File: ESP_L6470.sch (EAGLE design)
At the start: 39 parts, among them IC2 CP2104, J1 MICRO-USB, J2 POWER_JACKPTH_LOCK, Q1 600mA/40V, Q2 600mA/40V, U1 L6470, U2 ESP-WROOM-03, U3 RGB-LED

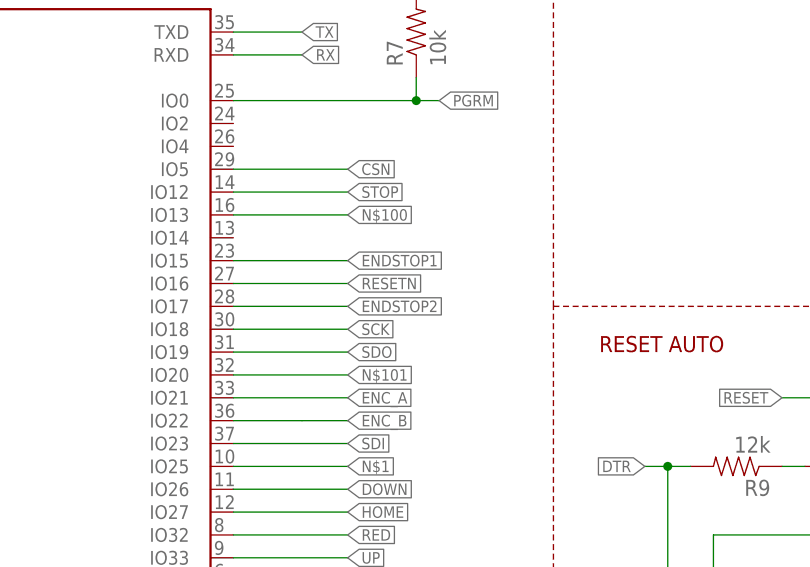
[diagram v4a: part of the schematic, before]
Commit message: Updated with silkscreen
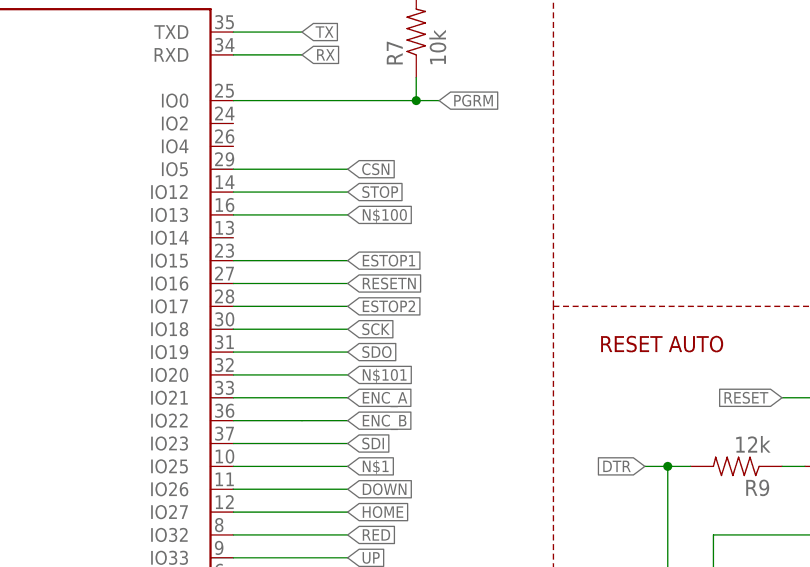
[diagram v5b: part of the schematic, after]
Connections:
- new net ESTOP1: U2.IO15
- new net ESTOP2: U2.IO17
- net ENDSTOP1: no longer U2.IO15
- net ENDSTOP2: no longer U2.IO17
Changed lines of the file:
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@@
 <label x="320.04" y="66.04" size="1.27" layer="95" rot="R180" xref="yes"/>
-</segment>
-<segment>
-<pinref part="U2" gate="G$1" pin="IO15"/>
-<wire x1="416.56" y1="142.24" x2="429.26" y2="142.24" width="0.1524" layer="91"/>
-<label x="429.26" y="142.24" size="1.27" layer="95" xref="yes"/>
 </segment>
 </net>
@@
 <wire x1="327.66" y1="48.26" x2="320.04" y2="48.26" width="0.1524" layer="91"/>
 <label x="320.04" y="48.26" size="1.27" layer="95" rot="R180" xref="yes"/>
-</segment>
-<segment>
-<pinref part="U2" gate="G$1" pin="IO17"/>
-<wire x1="416.56" y1="137.16" x2="429.26" y2="137.16" width="0.1524" layer="91"/>
-<label x="429.26" y="137.16" size="1.27" layer="95" xref="yes"/>
 </segment>
 </net>
@@
 </segment>
 </net>
+<net name="ESTOP1" class="0">
+<segment>
+<pinref part="U2" gate="G$1" pin="IO15"/>
+<wire x1="416.56" y1="142.24" x2="429.26" y2="142.24" width="0.1524" layer="91"/>
+<label x="429.26" y="142.24" size="1.27" layer="95" xref="yes"/>
+</segment>
+</net>
+<net name="ESTOP2" class="0">
+<segment>
+<pinref part="U2" gate="G$1" pin="IO17"/>
+<wire x1="416.56" y1="137.16" x2="429.26" y2="137.16" width="0.1524" layer="91"/>
+<label x="429.26" y="137.16" size="1.27" layer="95" xref="yes"/>
+</segment>
+</net>

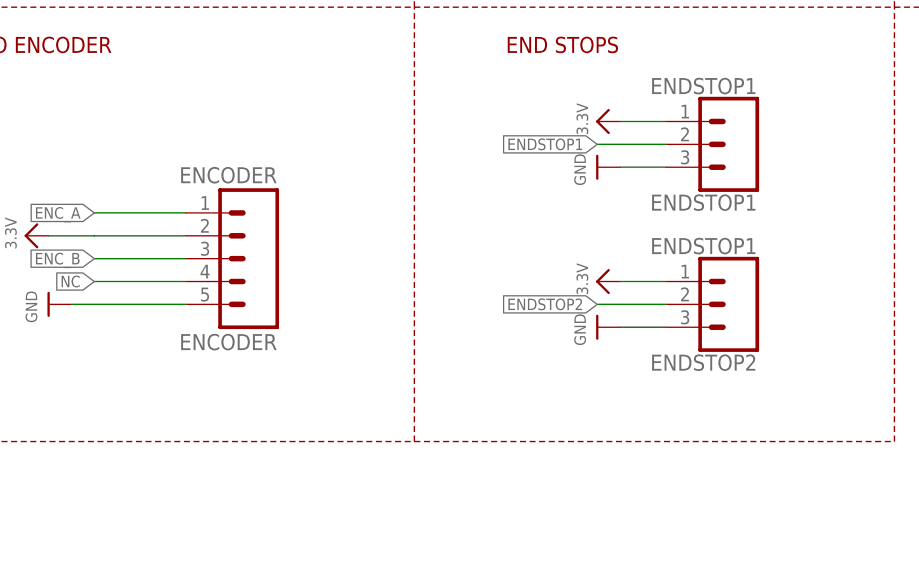
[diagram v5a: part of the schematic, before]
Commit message: renamed some parts
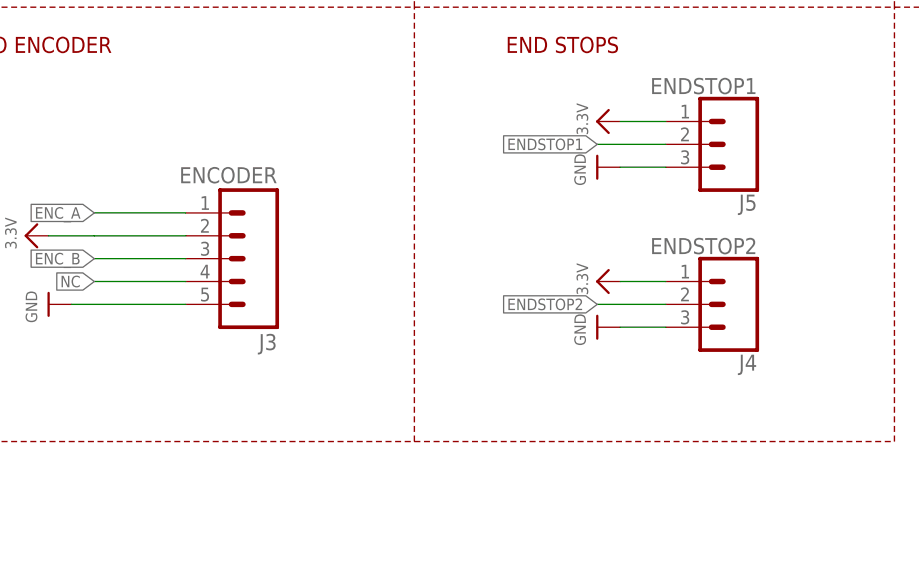
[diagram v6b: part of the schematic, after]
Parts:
- J4: value ENDSTOP1 -> ENDSTOP2
- renumbered ENCODER to J3, ENDSTOP1 to J5, ENDSTOP2 to J4, U$18 to S1, U$19 to S2, U$23 to S4, U$24 to S3
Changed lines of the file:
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@@
 <part name="R10" library="SparkFun-Passives" deviceset="RESISTOR" device="0603-RES" value="12k"/>
 <part name="U$14" library="microbuilder" deviceset="GND" device=""/>
-<part name="ENCODER" library="SparkFun-Connectors" deviceset="M05" device="PTH" value="ENCODER"/>
+<part name="J3" library="SparkFun-Connectors" deviceset="M05" device="PTH" value="ENCODER"/>
 <part name="U$20" library="microbuilder" deviceset="3.3V" device=""/>
 <part name="U$21" library="microbuilder" deviceset="GND" device=""/>
-<part name="ENDSTOP1" library="SparkFun-Connectors" deviceset="CONN_03" device="" value="ENDSTOP1"/>
-<part name="ENDSTOP2" library="SparkFun-Connectors" deviceset="CONN_03" device="" value="ENDSTOP1"/>
+<part name="J5" library="SparkFun-Connectors" deviceset="CONN_03" device="" value="ENDSTOP1"/>
+<part name="J4" library="SparkFun-Connectors" deviceset="CONN_03" device="" value="ENDSTOP2"/>
 <part name="U$1" library="microbuilder" deviceset="3.3V" device=""/>
 <part name="U$2" library="microbuilder" deviceset="3.3V" device=""/>
@@
 <part name="J2" library="SparkFun-Connectors" deviceset="POWER_JACK" device="PTH_LOCK"/>
 <part name="U$17" library="microbuilder" deviceset="3.3V" device=""/>
-<part name="U$18" library="IAD-Library" deviceset="B3AL-1002P-MS" device=""/>
-<part name="U$19" library="IAD-Library" deviceset="B3AL-1002P-MS" device=""/>
-<part name="U$23" library="IAD-Library" deviceset="B3AL-1002P-MS" device=""/>
-<part name="U$24" library="IAD-Library" deviceset="B3AL-1002P-MS" device=""/>
+<part name="S1" library="IAD-Library" deviceset="B3AL-1002P-MS" device=""/>
+<part name="S2" library="IAD-Library" deviceset="B3AL-1002P-MS" device=""/>
+<part name="S4" library="IAD-Library" deviceset="B3AL-1002P-MS" device=""/>
+<part name="S3" library="IAD-Library" deviceset="B3AL-1002P-MS" device=""/>
 <part name="IC2" library="microbuilder" deviceset="CP2104" device="" value="CP2104"/>
 <part name="U$33" library="microbuilder" deviceset="GND" device=""/>
@@
 <instance part="R10" gate="G$1" x="477.52" y="101.6" rot="R180"/>
 <instance part="U$14" gate="G$1" x="307.34" y="99.06" rot="R270"/>
-<instance part="ENCODER" gate="G$1" x="281.94" y="53.34" rot="R180"/>
+<instance part="J3" gate="G$1" x="281.94" y="53.34" rot="R180"/>
 <instance part="U$20" gate="G$1" x="256.54" y="55.88" rot="R90"/>
 <instance part="U$21" gate="G$1" x="259.08" y="48.26" rot="R270"/>
-<instance part="ENDSTOP1" gate="J$1" x="335.28" y="66.04" rot="R180"/>
-<instance part="ENDSTOP2" gate="J$1" x="335.28" y="48.26" rot="R180"/>
+<instance part="J5" gate="J$1" x="335.28" y="66.04" rot="R180"/>
+<instance part="J4" gate="J$1" x="335.28" y="48.26" rot="R180"/>
 <instance part="U$1" gate="G$1" x="320.04" y="68.58" rot="R90"/>
 <instance part="U$2" gate="G$1" x="320.04" y="50.8" rot="R90"/>
@@
 <instance part="J2" gate="G$1" x="68.58" y="5.08" rot="MR0"/>
 <instance part="U$17" gate="G$1" x="304.8" y="175.26"/>
-<instance part="U$18" gate="G$1" x="314.96" y="170.18"/>
-<instance part="U$19" gate="G$1" x="314.96" y="162.56"/>
-<instance part="U$23" gate="G$1" x="314.96" y="142.24"/>
-<instance part="U$24" gate="G$1" x="314.96" y="152.4"/>
+<instance part="S1" gate="G$1" x="314.96" y="170.18"/>
+<instance part="S2" gate="G$1" x="314.96" y="162.56"/>
+<instance part="S4" gate="G$1" x="314.96" y="142.24"/>
+<instance part="S3" gate="G$1" x="314.96" y="152.4"/>
 <instance part="IC2" gate="G$1" x="431.8" y="40.64"/>
 <instance part="U$33" gate="G$1" x="393.7" y="38.1" rot="R90"/>
@@
 </segment>
 <segment>
-<pinref part="ENCODER" gate="G$1" pin="5"/>
+<pinref part="J3" gate="G$1" pin="5"/>
 <pinref part="U$21" gate="G$1" pin="GND"/>
 <wire x1="274.32" y1="48.26" x2="261.62" y2="48.26" width="0.1524" layer="91"/>
 </segment>
 <segment>
-<pinref part="ENDSTOP2" gate="J$1" pin="3"/>
+<pinref part="J4" gate="J$1" pin="3"/>
 <pinref part="U$3" gate="G$1" pin="GND"/>
 <wire x1="322.58" y1="45.72" x2="327.66" y2="45.72" width="0.1524" layer="91"/>
 </segment>
 <segment>
-<pinref part="ENDSTOP1" gate="J$1" pin="3"/>
+<pinref part="J5" gate="J$1" pin="3"/>
 <pinref part="U$4" gate="G$1" pin="GND"/>
 <wire x1="322.58" y1="63.5" x2="327.66" y2="63.5" width="0.1524" layer="91"/>
@@
 </segment>
 <segment>
-<pinref part="ENCODER" gate="G$1" pin="2"/>
+<pinref part="J3" gate="G$1" pin="2"/>
 <pinref part="U$20" gate="G$1" pin="3.3V"/>
 <wire x1="274.32" y1="55.88" x2="264.16" y2="55.88" width="0.1524" layer="91"/>
@@
 </segment>
 <segment>
-<pinref part="ENDSTOP1" gate="J$1" pin="1"/>
+<pinref part="J5" gate="J$1" pin="1"/>
 <pinref part="U$1" gate="G$1" pin="3.3V"/>
 <wire x1="322.58" y1="68.58" x2="327.66" y2="68.58" width="0.1524" layer="91"/>
 </segment>
 <segment>
-<pinref part="ENDSTOP2" gate="J$1" pin="1"/>
+<pinref part="J4" gate="J$1" pin="1"/>
 <pinref part="U$2" gate="G$1" pin="3.3V"/>
 <wire x1="322.58" y1="50.8" x2="327.66" y2="50.8" width="0.1524" layer="91"/>
@@
 <junction x="304.8" y="162.56"/>
 <junction x="304.8" y="152.4"/>
-<pinref part="U$18" gate="G$1" pin="P$2"/>
-<pinref part="U$19" gate="G$1" pin="P$2"/>
-<pinref part="U$24" gate="G$1" pin="P$2"/>
-<pinref part="U$23" gate="G$1" pin="P$2"/>
+<pinref part="S1" gate="G$1" pin="P$2"/>
+<pinref part="S2" gate="G$1" pin="P$2"/>
+<pinref part="S3" gate="G$1" pin="P$2"/>
+<pinref part="S4" gate="G$1" pin="P$2"/>
 </segment>
 <segment>
@@
 <net name="ENDSTOP1" class="0">
 <segment>
-<pinref part="ENDSTOP1" gate="J$1" pin="2"/>
+<pinref part="J5" gate="J$1" pin="2"/>
 <wire x1="327.66" y1="66.04" x2="320.04" y2="66.04" width="0.1524" layer="91"/>
 <label x="320.04" y="66.04" size="1.27" layer="95" rot="R180" xref="yes"/>
@@
 <net name="ENDSTOP2" class="0">
 <segment>
-<pinref part="ENDSTOP2" gate="J$1" pin="2"/>
+<pinref part="J4" gate="J$1" pin="2"/>
 <wire x1="327.66" y1="48.26" x2="320.04" y2="48.26" width="0.1524" layer="91"/>
 <label x="320.04" y="48.26" size="1.27" layer="95" rot="R180" xref="yes"/>
@@
 <net name="ENC_A" class="0">
 <segment>
-<pinref part="ENCODER" gate="G$1" pin="1"/>
+<pinref part="J3" gate="G$1" pin="1"/>
 <wire x1="274.32" y1="58.42" x2="264.16" y2="58.42" width="0.1524" layer="91"/>
 <label x="264.16" y="58.42" size="1.27" layer="95" rot="R180" xref="yes"/>
@@
 <net name="ENC_B" class="0">
 <segment>
-<pinref part="ENCODER" gate="G$1" pin="3"/>
+<pinref part="J3" gate="G$1" pin="3"/>
 <wire x1="274.32" y1="53.34" x2="264.16" y2="53.34" width="0.1524" layer="91"/>
 <label x="264.16" y="53.34" size="1.27" layer="95" rot="R180" xref="yes"/>
@@
 <net name="NC" class="0">
 <segment>
-<pinref part="ENCODER" gate="G$1" pin="4"/>
+<pinref part="J3" gate="G$1" pin="4"/>
 <wire x1="274.32" y1="50.8" x2="264.16" y2="50.8" width="0.1524" layer="91"/>
 <label x="264.16" y="50.8" size="1.27" layer="95" rot="R180" xref="yes"/>
@@
 <wire x1="322.58" y1="170.18" x2="330.2" y2="170.18" width="0.1524" layer="91"/>
 <label x="330.2" y="170.18" size="1.4224" layer="95" xref="yes"/>
-<pinref part="U$18" gate="G$1" pin="P$1"/>
+<pinref part="S1" gate="G$1" pin="P$1"/>
 </segment>
 <segment>
@@
 <wire x1="322.58" y1="162.56" x2="330.2" y2="162.56" width="0.1524" layer="91"/>
 <label x="330.2" y="162.56" size="1.4224" layer="95" xref="yes"/>
-<pinref part="U$19" gate="G$1" pin="P$1"/>
+<pinref part="S2" gate="G$1" pin="P$1"/>
 </segment>
 <segment>
@@
 <wire x1="322.58" y1="152.4" x2="330.2" y2="152.4" width="0.1524" layer="91"/>
 <label x="330.2" y="152.4" size="1.4224" layer="95" xref="yes"/>
-<pinref part="U$24" gate="G$1" pin="P$1"/>
+<pinref part="S3" gate="G$1" pin="P$1"/>
 </segment>
 <segment>
@@
 <wire x1="322.58" y1="142.24" x2="330.2" y2="142.24" width="0.1524" layer="91"/>
 <label x="330.2" y="142.24" size="1.4224" layer="95" xref="yes"/>
-<pinref part="U$23" gate="G$1" pin="P$1"/>
-</segment>
-<segment>
+<pinref part="S4" gate="G$1" pin="P$1"/>
+</segment>
+<segment>

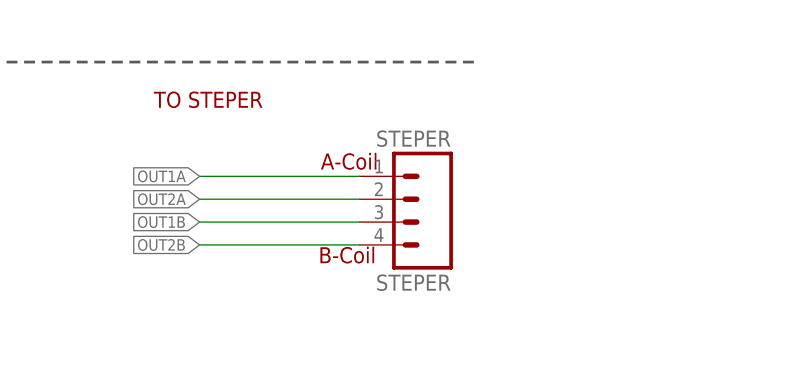
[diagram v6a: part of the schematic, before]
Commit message: renamed some parts
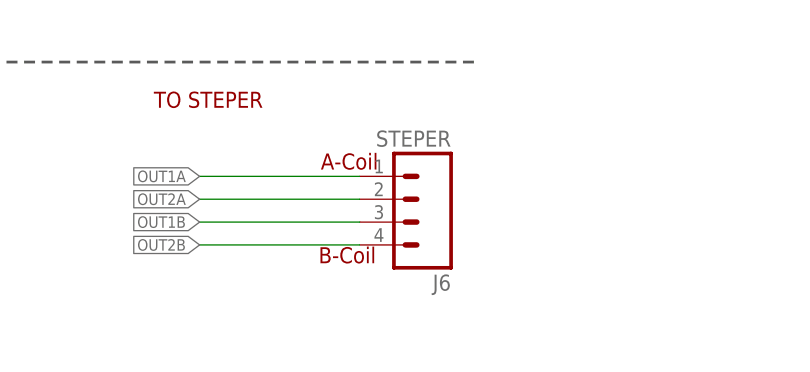
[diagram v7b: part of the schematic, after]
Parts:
- renumbered STEPER to J6, U$5 to U4
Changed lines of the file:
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@@
 <part name="VS" library="SparkFun" deviceset="VCC" device="" value="VS"/>
 <part name="U$8" library="microbuilder" deviceset="3.3V" device=""/>
-<part name="U$5" library="IAD_ZHDK" deviceset="TRACO12433" device=""/>
-<part name="STEPER" library="SparkFun-Connectors" deviceset="M04" device="LOCK_LONGPADS" value="STEPER"/>
+<part name="U4" library="IAD_ZHDK" deviceset="TRACO12433" device=""/>
+<part name="J6" library="SparkFun-Connectors" deviceset="M04" device="LOCK_LONGPADS" value="STEPER"/>
 <part name="J2" library="SparkFun-Connectors" deviceset="POWER_JACK" device="PTH_LOCK"/>
 <part name="U$17" library="microbuilder" deviceset="3.3V" device=""/>
@@
 <instance part="VS" gate="1" x="309.88" y="104.14" rot="R90"/>
 <instance part="U$8" gate="G$1" x="307.34" y="93.98" rot="R90"/>
-<instance part="U$5" gate="G$1" x="320.04" y="104.14"/>
-<instance part="STEPER" gate="G$1" x="139.7" y="20.32" rot="R180"/>
+<instance part="U4" gate="G$1" x="320.04" y="104.14"/>
+<instance part="J6" gate="G$1" x="139.7" y="20.32" rot="R180"/>
 <instance part="J2" gate="G$1" x="68.58" y="5.08" rot="MR0"/>
 <instance part="U$17" gate="G$1" x="304.8" y="175.26"/>
@@
 <wire x1="320.04" y1="99.06" x2="309.88" y2="99.06" width="0.1524" layer="91"/>
 <pinref part="U$14" gate="G$1" pin="GND"/>
-<pinref part="U$5" gate="G$1" pin="GND"/>
+<pinref part="U4" gate="G$1" pin="GND"/>
 </segment>
 <segment>
@@
 <wire x1="134.62" y1="22.86" x2="116.84" y2="22.86" width="0.1524" layer="91"/>
 <label x="116.84" y="22.86" size="1.27" layer="95" rot="MR0" xref="yes"/>
-<pinref part="STEPER" gate="G$1" pin="1"/>
+<pinref part="J6" gate="G$1" pin="1"/>
 </segment>
 </net>
@@
 <wire x1="134.62" y1="20.32" x2="116.84" y2="20.32" width="0.1524" layer="91"/>
 <label x="116.84" y="20.32" size="1.27" layer="95" rot="MR0" xref="yes"/>
-<pinref part="STEPER" gate="G$1" pin="2"/>
+<pinref part="J6" gate="G$1" pin="2"/>
 </segment>
 </net>
@@
 <wire x1="134.62" y1="17.78" x2="116.84" y2="17.78" width="0.1524" layer="91"/>
 <label x="116.84" y="17.78" size="1.27" layer="95" rot="R180" xref="yes"/>
-<pinref part="STEPER" gate="G$1" pin="3"/>
+<pinref part="J6" gate="G$1" pin="3"/>
 </segment>
 </net>
@@
 <wire x1="134.62" y1="15.24" x2="116.84" y2="15.24" width="0.1524" layer="91"/>
 <label x="116.84" y="15.24" size="1.27" layer="95" rot="R180" xref="yes"/>
-<pinref part="STEPER" gate="G$1" pin="4"/>
+<pinref part="J6" gate="G$1" pin="4"/>
 </segment>
 </net>
@@
 <wire x1="312.42" y1="93.98" x2="309.88" y2="93.98" width="0.1524" layer="91"/>
 <pinref part="U$8" gate="G$1" pin="3.3V"/>
-<pinref part="U$5" gate="G$1" pin="3.3VOUT"/>
+<pinref part="U4" gate="G$1" pin="3.3VOUT"/>
 </segment>
 <segment>
@@
 <pinref part="VS" gate="1" pin="VCC"/>
 <wire x1="309.88" y1="104.14" x2="320.04" y2="104.14" width="0.1524" layer="91"/>
-<pinref part="U$5" gate="G$1" pin="VIN"/>
-</segment>
-</net>
+<pinref part="U4" gate="G$1" pin="VIN"/>
+</segment>
+</net>
